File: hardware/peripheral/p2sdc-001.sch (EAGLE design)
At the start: 72 parts, among them IC1 74LS06N, IC2 4066N, J1 MKR, J10 1-Wire, J2 GPIO, J3 Vcc, J4** RLY2, J5 SPI, J6 LED, J7 DIN5, J8 DIN5, J9 DIN5, K1 G5V1, Q1 220mA/50V/3.5Ω, Q2 220mA/50V/3.5Ω, T1 2SC1815, U1 DS18B20

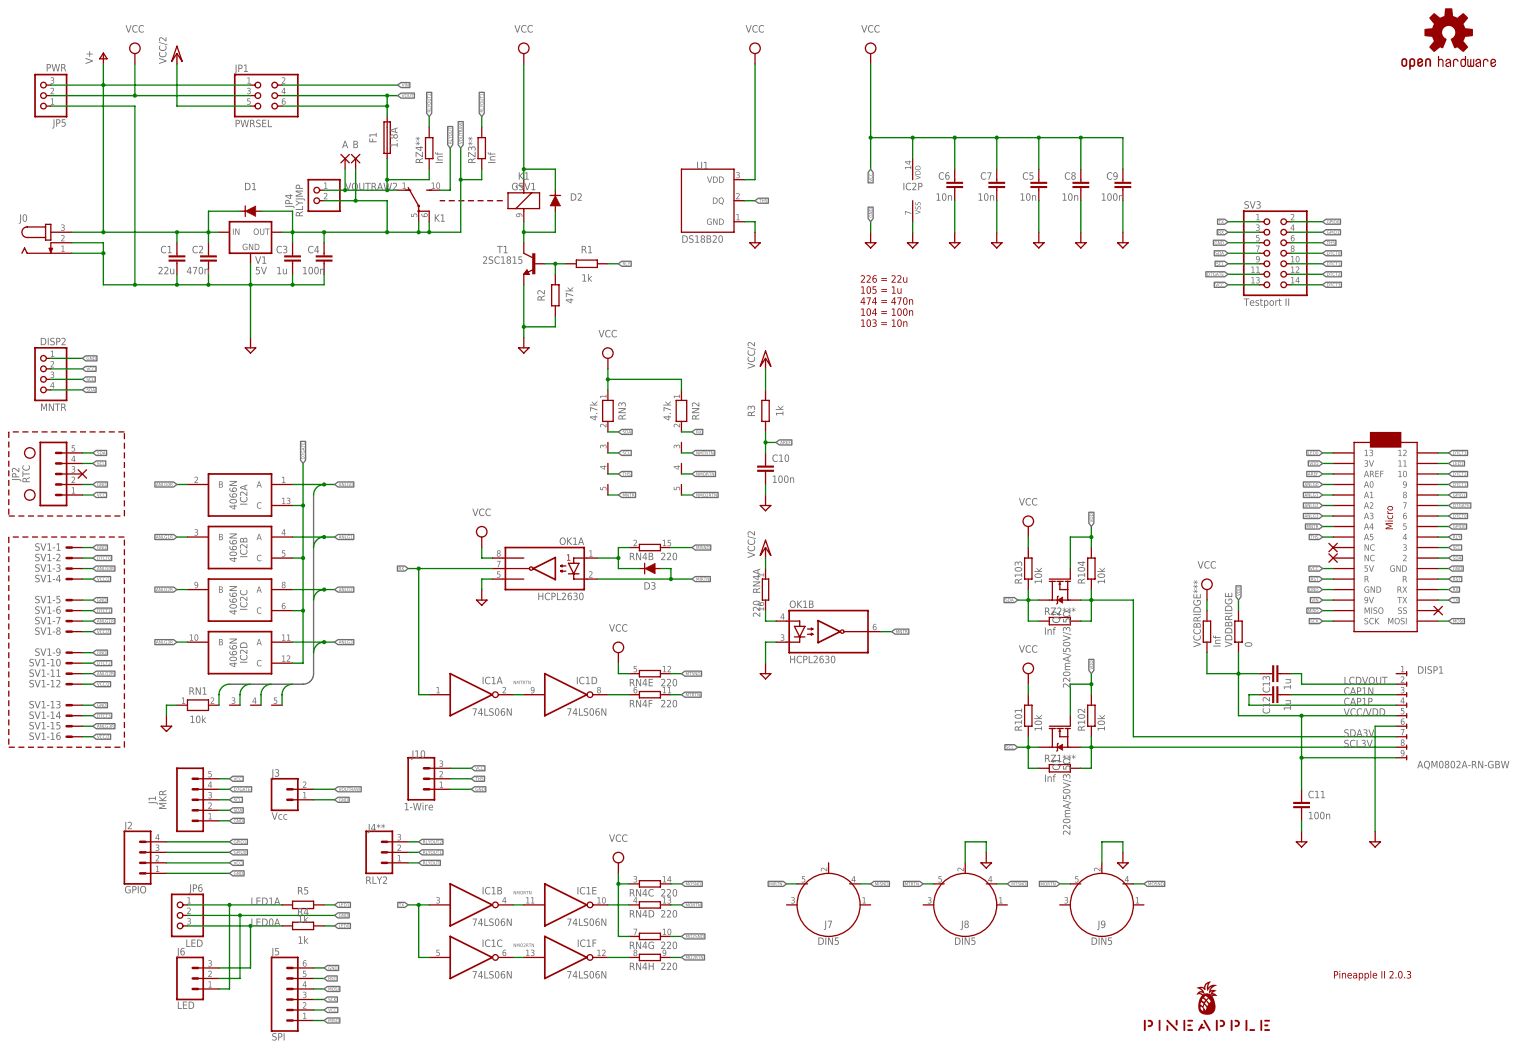
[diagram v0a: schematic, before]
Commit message: Removed parts.
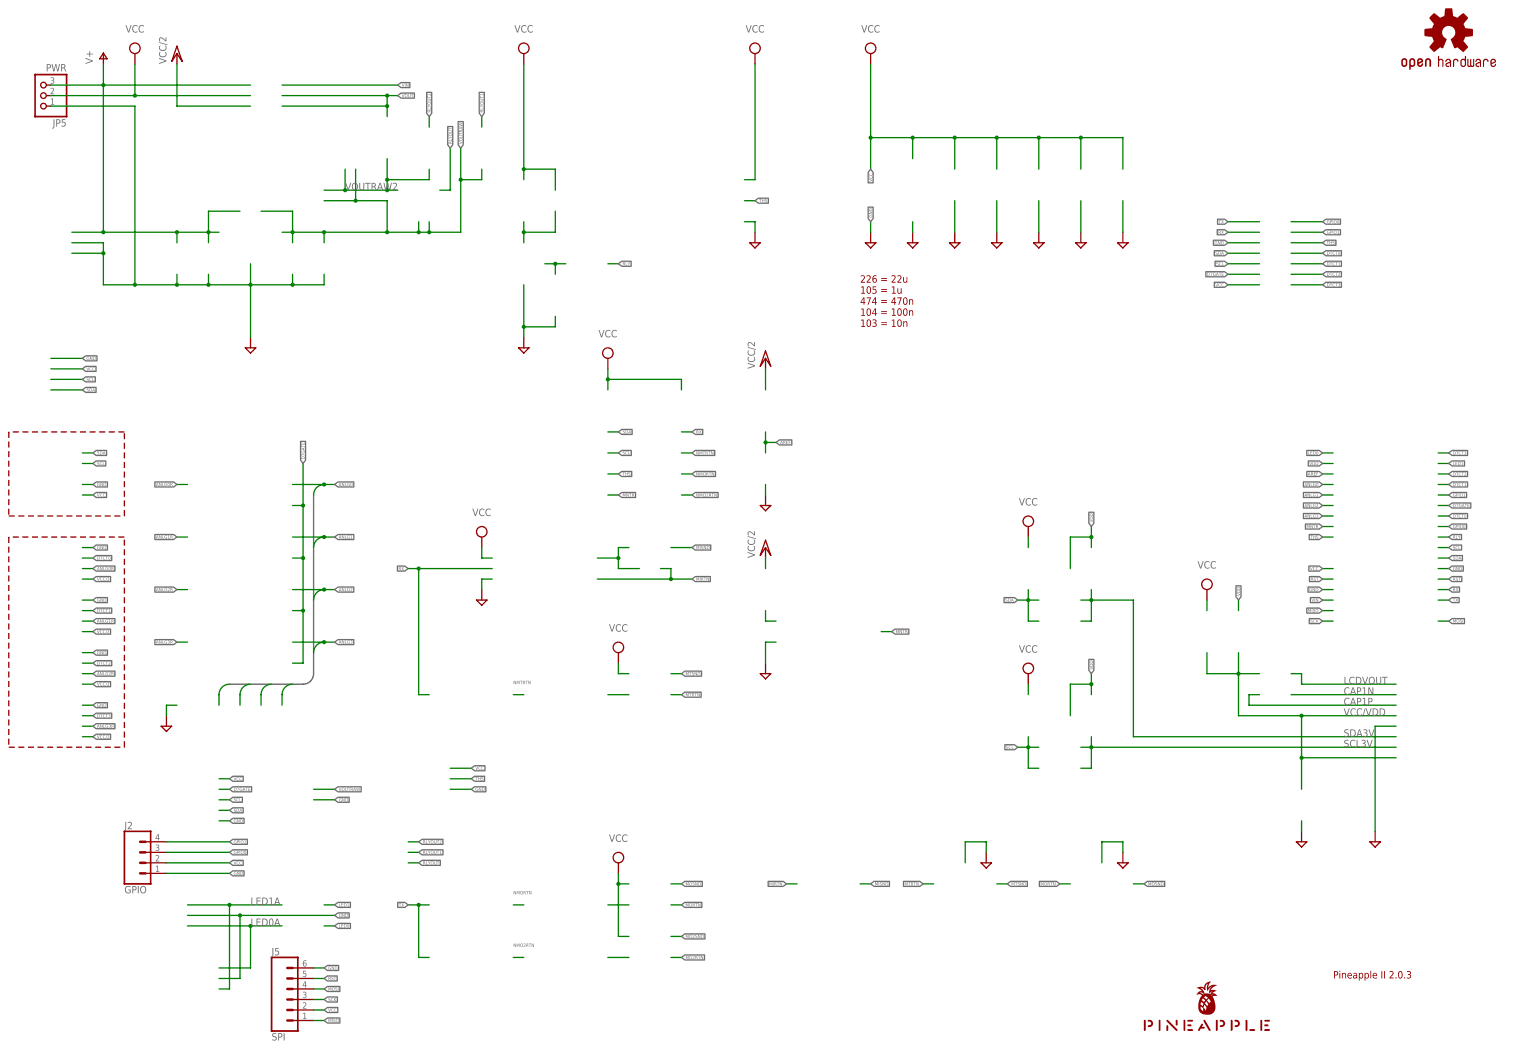
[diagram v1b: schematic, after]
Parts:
- removed A, B: (no value), wirepad:SMD2
- removed C1: 22u, rcl:C-EU025-050X050
- removed C10, C11, C4: 100n, rcl:C-EU025-024X044
- removed C12, C13, C3: 1u, rcl:C-EU050-024X044
- removed C2: 470n, rcl:C-EU050-024X044
- removed C5, C6, C7, C8: 10n, resistor:C-EU025-024X044
- removed C9: 100n, resistor:C-EU025-024X044
- removed D1, D2, D3: DIODE-1N4148, SparkFun-DiscreteSemi:DIODE-1N4148
- removed DISP1: AQM0802A-RN-GBW, AQM0802A-RN-GBW:AQM0802A-RN-GBW
- removed DISP2: MNTR, pinhead:PINHD-1X4
- removed F1: 1.8A, fuse:TE5
- removed H1, H2: STAND-OFF, SparkFun-Hardware:STAND-OFF
- removed IC1: 74LS06N, 74xx-us:74LS06N
- removed IC2: 4066N, 40xx:4066N
- removed J0: (no value), con-jack:JACK-PLUG0
- removed J1: MKR, SparkFun-Connectors:CONN_05JST
- removed J10: 1-Wire, SparkFun-Connectors:CONN_03JST-PTH-VERT
- removed J3: Vcc, SparkFun-Connectors:CONN_02JST-PTH-2
- removed J4**: RLY2, SparkFun-Connectors:CONN_03JST-PTH-NS
- removed J6: LED, SparkFun-Connectors:CONN_03JST-PTH-VERT
- removed J7, J8, J9: DIN5, SparkFun-Connectors:DIN5
- removed JP1: PWRSEL, pinhead:PINHD-2X3
- removed JP2: RTC, SparkFun-Connectors:CONN_05
- removed JP4: RLYJMP, pinhead:PINHD-1X2
- removed JP6: LED, pinhead:PINHD-1X3
- removed K1: G5V1, relay:G5V1
- removed MC1: ARDUINOMICRO, adafruit:ARDUINOMICRO
- removed OK1: HCPL2630, optocoupler:HCPL2630
- removed Q1, Q2: 220mA/50V/3.5Ω, SparkFun-DiscreteSemi:MOSFET-NCH-BSS138
- removed R1, R3, R4, R5: 1k, resistor:R-EU_0204/5
- removed R101, R102, R103, R104: 10k, rcl:R-EU_M2012
- removed R2: 47k, resistor:R-EU_0204/5
- removed RN1: 10k, resistor-net:RN04
- removed RN2, RN3: 4.7k, resistor-net:RN04
- removed RN4: 220, resistor-dil:8R-N
- removed RZ1***, RZ2***, RZ3**, RZ4**, VCCBRIDGE***: Inf, rcl:R-EU_M2012
- removed SV1: (no value), con-ml:ML16LE
- removed SV3: Testport II, pinhead:PINHD-2X7
- removed T1: 2SC1815, transistor:2SC1815
- removed U1: DS18B20, SparkFun-Sensors:DS18B20
- removed V1: 5V, v-reg:78XXL
- removed VDDBRIDGE: 0, rcl:R-EU_M2012
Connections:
- removed net ANLG0: IC2A.A, MC1.A0, RN1.2
- removed net ANLG0R: IC2A.B, SV1-3.S
- removed net ANLG1: IC2B.A, MC1.A1, RN1.3
- removed net ANLG1R: IC2B.B, SV1-7.S
- removed net ANLG2: IC2C.A, MC1.A2, RN1.4
- removed net ANLG2R: IC2C.B, SV1-11.S
- removed net ANLG3: IC2D.A, MC1.A3, RN1.5
- removed net ANLG3R: IC2D.B, SV1-15.S
- removed net AREF: C10.1, MC1.AREF, R3.1
- removed net CAP1N: C12.2, DISP1.3
- removed net CAP1P: C12.1, DISP1.4
- removed net D7GATE: IC2A.C, IC2B.C, IC2C.C, IC2D.C, J1.4, MC1.7, SV3.11
- removed net DTCT0: MC1.6, SV1-2.S, SV3.8
- removed net DTCT1: MC1.9, SV1-6.S, SV3.10
- removed net DTCT2: MC1.10, SV1-10.S, SV3.12
- removed net DTCT3: MC1.12, SV1-14.S, SV3.14
- removed net LCDVOUT: C13.2, DISP1.2
- removed net LED0: MC1.13, R4.2
- removed net LED0A: J6.3, JP6.3, R4.1
- removed net LED1: MC1.11, R5.2
- removed net LED1A: J6.1, JP6.1, R5.1
- removed net MIDIINSND: D3.C, OK1A.A1, RN4B.1
- removed net MIRTN: D3.A, J7.5, OK1A.C1
- removed net MISND: J7.4, RN4B.2
- removed net MNTR: MC1.A4, OK1B.VO2, RN3.5
- removed net MNTRA: OK1B.A2, RN4A.2
- removed net MO2RTN: RN4H.2
- removed net MO2RTNRAW: IC1F.O, RN4H.1
- removed net MO2SND: RN4G.2
- removed net MORTN: J9.5, RN4D.2
- removed net MORTNRAW: IC1E.O, RN4D.1
- removed net MOSND: J9.4, RN4C.2
- removed net MTRTN: J8.5, RN4F.2
- removed net MTRTNRAW: IC1D.O, RN4F.1
- removed net MTSND: J8.4, RN4E.2
- removed net NMO2RTN: IC1C.O, IC1F.I, RN2.5
- removed net NMORTN: IC1B.O, IC1E.I, RN2.4
- removed net NMTRTN: IC1A.O, IC1D.I, RN2.3
- removed net RLY: MC1.4, R1.2
- removed net RLYDRV: R1.1, R2.2, T1.B
- removed net RLYOUT: J4**.1, K12.S
- removed net RLYOUT1: J4**.2, RZ3**.2
- removed net RLYOUT2: J4**.3, RZ4**.2
- removed net RLYSNK: D2.A, K11.2, T1.C
- removed net RX: IC1A.I, MC1.RX, OK1A.VO1, RN2.2, SV3.3
- removed net SCL: DISP2.3, J1.3, JP2.4, MC1.3, Q1.D, R101.1, RN3.3, RZ1***.1, SV3.9
- removed net SCL3V: DISP1.8, Q1.S, R102.1, RZ1***.2
- removed net SDA: DISP2.4, J1.2, JP2.5, MC1.2, Q2.D, R103.1, RN3.2, RZ2***.1, SV3.7
- removed net SDA3V: DISP1.7, Q2.S, R104.1, RZ2***.2
- removed net THS: J10.2, MC1.A5, RN3.4, SV3.6, U1.DQ
- removed net TX: IC1B.I, IC1C.I, MC1.TX, SV3.1
- removed net VCC/2: JP1.5, R3.2, RN4A.1, SV1-12.S, SV1-16.S, SV1-4.S, SV1-8.S
- removed net VCC/VDD: C11.1, C13.1, DISP1.5, DISP1.9, VCCBRIDGE***.1, VDDBRIDGE.1
- removed net VDD: MC1.3V, Q1.G, Q2.G, R102.2, R104.2, VDDBRIDGE.2
- removed net VIN: JP1.2, MC1.9V
- removed net VOUT: F1.2, JP1.4, JP1.6
- removed net VOUTRAW: B.P, C3.1, C4.1, D1.A, J3.2, JP4.2, K12.P, K12.P@1, RZ3**.1, V1.OUT
- removed net VOUTRAW2: A.P, F1.1, JP4.1, K12.O, RZ4**.1
- net GND: no longer C1.2, C10.2, C11.2, C2.2, C3.2, C4.2, C5.2, C6.2, C7.2, C8.2, C9.2, DISP1.6, DISP2.1, IC2P.VSS, J0.1, J0.2, J1.1, J10.1, J3.1, J6.2, J8.2, J9.2, JP2.2, JP6.2, MC1.GND, MC1.GND@1, OK1A.GND, OK1B.C2, R2.1, RN1.1, SV1-1.S, SV1-13.S, SV1-5.S, SV1-9.S, SV3.5, T1.E, U1.GND, V1.GND
- net GPIO0: no longer MC1.5, SV3.2
- net GPIO1: no longer MC1.8, SV3.4
- net MISO: no longer MC1.MISO
- net MOSI: no longer MC1.MOSI
- net RST: no longer MC1.R@1, MC1.R@2
- net SCK: no longer MC1.SCK
- net V+: no longer C1.1, C2.1, D1.C, J0.3, JP1.1, V1.IN
- net VCC: no longer C5.1, C6.1, C7.1, C8.1, C9.1, D2.C, DISP2.2, IC2P.VDD, J1.5, J10.3, JP1.3, JP2.1, K11.1, MC1.5V, OK1A.VCC, R101.2, R103.2, RN2.1, RN3.1, RN4C.1, RN4E.1, RN4G.1, SV3.13, U1.VDD, VCCBRIDGE***.2

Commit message: Positioning of the breakout card.
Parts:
- added JP1: (no value), pinhead:PINHD-1X8
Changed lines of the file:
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@@
 <part name="J2" library="SparkFun-Connectors" library_urn="urn:adsk.eagle:library:513" deviceset="CONN_04" device="JST-PTH" package3d_urn="urn:adsk.eagle:package:38101/1" value="GPIO"/>
 <part name="J5" library="SparkFun-Connectors" library_urn="urn:adsk.eagle:library:513" deviceset="CONN_06" device="1.27MM" package3d_urn="urn:adsk.eagle:package:38131/1" value="SPI"/>
+<part name="JP1" library="pinhead" library_urn="urn:adsk.eagle:library:325" deviceset="PINHD-1X8" device="" package3d_urn="urn:adsk.eagle:package:22409/2"/>
 </parts>
 <sheets>
@@
 <attribute name="NAME" x="86.36" y="25.908" size="1.778" layer="95" font="vector"/>
 </instance>
+<instance part="JP1" gate="A" x="30.48" y="30.48" smashed="yes" rot="R180">
+<attribute name="NAME" x="36.83" y="17.145" size="1.778" layer="95" rot="R180"/>
+<attribute name="VALUE" x="36.83" y="43.18" size="1.778" layer="96" rot="R180"/>
+</instance>
 </instances>

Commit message: First try.
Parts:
- added R1: 10k, resistor:R-EU_0204/5
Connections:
- net GND: now also JP1.3
- net GPIO0: now also JP1.7
- net GPIO1: now also JP1.8, R1.1
- net MISO: now also JP1.5
- net MOSI: now also JP1.6
- net SCK: now also JP1.4
- net VCC: now also JP1.1, R1.2
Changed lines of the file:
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@@
 <part name="J5" library="SparkFun-Connectors" library_urn="urn:adsk.eagle:library:513" deviceset="CONN_06" device="1.27MM" package3d_urn="urn:adsk.eagle:package:38131/1" value="SPI"/>
 <part name="JP1" library="pinhead" library_urn="urn:adsk.eagle:library:325" deviceset="PINHD-1X8" device="" package3d_urn="urn:adsk.eagle:package:22409/2"/>
+<part name="R1" library="resistor" library_urn="urn:adsk.eagle:library:348" deviceset="R-EU_" device="0204/5" package3d_urn="urn:adsk.eagle:package:23488/1" value="10k"/>
 </parts>
 <sheets>
@@
 <attribute name="VALUE" x="36.83" y="43.18" size="1.778" layer="96" rot="R180"/>
 </instance>
+<instance part="R1" gate="G$1" x="40.64" y="48.26" smashed="yes" rot="R90">
+<attribute name="NAME" x="39.1414" y="44.45" size="1.778" layer="95" rot="R90"/>
+<attribute name="VALUE" x="43.942" y="44.45" size="1.778" layer="96" rot="R90"/>
+</instance>
 </instances>
 <busses>
@@
 <label x="134.62" y="66.04" size="0.8128" layer="95" xref="yes"/>
 </segment>
+<segment>
+<pinref part="JP1" gate="A" pin="3"/>
+<wire x1="33.02" y1="25.4" x2="43.18" y2="25.4" width="0.1524" layer="91"/>
+<label x="43.18" y="25.4" size="0.8128" layer="95" xref="yes"/>
+</segment>
 </net>
 <net name="VCC" class="2">
@@
 <label x="134.62" y="71.12" size="0.8128" layer="95" xref="yes"/>
 </segment>
+<segment>
+<pinref part="JP1" gate="A" pin="1"/>
+<wire x1="33.02" y1="20.32" x2="43.18" y2="20.32" width="0.1524" layer="91"/>
+<label x="43.18" y="20.32" size="0.8128" layer="95" xref="yes"/>
+</segment>
+<segment>
+<pinref part="R1" gate="G$1" pin="2"/>
+<wire x1="40.64" y1="53.34" x2="40.64" y2="58.42" width="0.1524" layer="91"/>
+<label x="40.64" y="58.42" size="0.8128" layer="95" rot="R90" xref="yes"/>
+</segment>
 </net>
 <net name="MIDIINSND" class="0">
@@
 <label x="340.36" y="200.66" size="0.8128" layer="95" xref="yes"/>
 </segment>
+<segment>
+<pinref part="JP1" gate="A" pin="8"/>
+<wire x1="33.02" y1="38.1" x2="40.64" y2="38.1" width="0.1524" layer="91"/>
+<label x="43.18" y="38.1" size="0.8128" layer="95" xref="yes"/>
+<pinref part="R1" gate="G$1" pin="1"/>
+<wire x1="40.64" y1="38.1" x2="43.18" y2="38.1" width="0.1524" layer="91"/>
+<wire x1="40.64" y1="43.18" x2="40.64" y2="38.1" width="0.1524" layer="91"/>
+<junction x="40.64" y="38.1"/>
+</segment>
 </net>
 <net name="GPIO0" class="0">
@@
 <wire x1="332.74" y1="203.2" x2="340.36" y2="203.2" width="0.1524" layer="91"/>
 <label x="340.36" y="203.2" size="0.8128" layer="95" xref="yes"/>
+</segment>
+<segment>
+<pinref part="JP1" gate="A" pin="7"/>
+<wire x1="33.02" y1="35.56" x2="43.18" y2="35.56" width="0.1524" layer="91"/>
+<label x="43.18" y="35.56" size="0.8128" layer="95" xref="yes"/>
 </segment>
 </net>
@@
 <label x="99.06" y="10.16" size="0.8128" layer="95" xref="yes"/>
 </segment>
+<segment>
+<pinref part="JP1" gate="A" pin="5"/>
+<wire x1="33.02" y1="30.48" x2="43.18" y2="30.48" width="0.1524" layer="91"/>
+<label x="43.18" y="30.48" size="0.8128" layer="95" xref="yes"/>
+</segment>
 </net>
 <net name="SCK" class="0">
@@
 <pinref part="J5" gate="G$1" pin="3"/>
 </segment>
+<segment>
+<pinref part="JP1" gate="A" pin="4"/>
+<wire x1="33.02" y1="27.94" x2="43.18" y2="27.94" width="0.1524" layer="91"/>
+<label x="43.18" y="27.94" size="0.8128" layer="95" xref="yes"/>
+</segment>
 </net>
 <net name="MOSI" class="0">
@@
 <pinref part="J5" gate="G$1" pin="4"/>
 </segment>
-</net>
+<segment>
+<pinref part="JP1" gate="A" pin="6"/>
+<wire x1="33.02" y1="33.02" x2="43.18" y2="33.02" width="0.1524" layer="91"/>
+<label x="43.18" y="33.02" size="0.8128" layer="95" xref="yes"/>
+</segment>
+</net>

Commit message: New interface.
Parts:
- removed J2: GPIO, SparkFun-Connectors:CONN_04JST-PTH
- added J1: (no value), SparkFun-Connectors:CONN_041.27MM
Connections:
- net GND: no longer J2.1
- net GPIO0: now also J1.3; no longer J2.3
- net GPIO1: now also J1.4; no longer J2.4
- net VCC: no longer J2.2
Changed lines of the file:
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@@
 <part name="SUPPLY24" library="supply2" library_urn="urn:adsk.eagle:library:372" deviceset="VCC" device=""/>
 <part name="SUPPLY25" library="supply2" library_urn="urn:adsk.eagle:library:372" deviceset="VCC" device=""/>
-<part name="J2" library="SparkFun-Connectors" library_urn="urn:adsk.eagle:library:513" deviceset="CONN_04" device="JST-PTH" package3d_urn="urn:adsk.eagle:package:38101/1" value="GPIO"/>
 <part name="J5" library="SparkFun-Connectors" library_urn="urn:adsk.eagle:library:513" deviceset="CONN_06" device="1.27MM" package3d_urn="urn:adsk.eagle:package:38131/1" value="SPI"/>
 <part name="JP1" library="pinhead" library_urn="urn:adsk.eagle:library:325" deviceset="PINHD-1X8" device="" package3d_urn="urn:adsk.eagle:package:22409/2"/>
 <part name="R1" library="resistor" library_urn="urn:adsk.eagle:library:348" deviceset="R-EU_" device="0204/5" package3d_urn="urn:adsk.eagle:package:23488/1" value="10k"/>
+<part name="J1" library="SparkFun-Connectors" library_urn="urn:adsk.eagle:library:513" deviceset="CONN_04" device="1.27MM" package3d_urn="urn:adsk.eagle:package:38086/1"/>
 </parts>
 <sheets>
@@
 <attribute name="VALUE" x="312.42" y="119.38" size="1.778" layer="96" align="bottom-center"/>
 </instance>
-<instance part="J2" gate="G$1" x="55.88" y="48.26" smashed="yes">
-<attribute name="VALUE" x="50.8" y="40.894" size="1.778" layer="96" font="vector"/>
-<attribute name="NAME" x="50.8" y="56.388" size="1.778" layer="95" font="vector"/>
-</instance>
 <instance part="J5" gate="G$1" x="91.44" y="15.24" smashed="yes">
 <attribute name="VALUE" x="86.36" y="5.334" size="1.778" layer="96" font="vector"/>
@@
 <attribute name="NAME" x="39.1414" y="44.45" size="1.778" layer="95" rot="R90"/>
 <attribute name="VALUE" x="43.942" y="44.45" size="1.778" layer="96" rot="R90"/>
+</instance>
+<instance part="J1" gate="G$1" x="55.88" y="48.26" smashed="yes">
+<attribute name="VALUE" x="50.8" y="40.894" size="1.778" layer="96" font="vector"/>
+<attribute name="NAME" x="50.8" y="56.388" size="1.778" layer="95" font="vector"/>
 </instance>
 </instances>
@@
 </segment>
 <segment>
-<label x="76.2" y="45.72" size="0.8128" layer="95" xref="yes"/>
-<pinref part="J2" gate="G$1" pin="1"/>
-<wire x1="76.2" y1="45.72" x2="60.96" y2="45.72" width="0.1524" layer="91"/>
-</segment>
-<segment>
 <wire x1="73.66" y1="58.42" x2="76.2" y2="58.42" width="0.1524" layer="91"/>
 <label x="76.2" y="58.42" size="0.8128" layer="95" xref="yes"/>
@@
 </segment>
 <segment>
-<pinref part="J2" gate="G$1" pin="2"/>
-<wire x1="60.96" y1="48.26" x2="76.2" y2="48.26" width="0.1524" layer="91"/>
-<label x="76.2" y="48.26" size="0.8128" layer="95" xref="yes"/>
-</segment>
-<segment>
 <wire x1="96.52" y1="12.7" x2="99.06" y2="12.7" width="0.1524" layer="91"/>
 <label x="99.06" y="12.7" size="0.8128" layer="95" xref="yes"/>
@@
 <wire x1="60.96" y1="53.34" x2="76.2" y2="53.34" width="0.1524" layer="91"/>
 <label x="76.2" y="53.34" size="0.8128" layer="95" xref="yes"/>
-<pinref part="J2" gate="G$1" pin="4"/>
+<pinref part="J1" gate="G$1" pin="4"/>
 </segment>
 <segment>
@@
 <wire x1="60.96" y1="50.8" x2="76.2" y2="50.8" width="0.1524" layer="91"/>
 <label x="76.2" y="50.8" size="0.8128" layer="95" xref="yes"/>
-<pinref part="J2" gate="G$1" pin="3"/>
-</segment>
-<segment>
+<pinref part="J1" gate="G$1" pin="3"/>
+</segment>
+<segment>
